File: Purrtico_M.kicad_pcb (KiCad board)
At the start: 2 copper layers, 53 parts, among them J2 Conn_01x02, J3 Conn_01x03, J4 Conn_01x02, U1 OPA1679, U2 OPA1679

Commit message: update pcb
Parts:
- moved R5 89.9 mm to (150.5, 33.7)
- moved R19 82.6 mm to (160.0, 35.6), turned to 180 degrees
- moved R20 72.9 mm to (155.6, 47.6), turned to 180 degrees
- moved R14 67.4 mm to (154.9, 56.5), turned to 180 degrees
- moved R10 65.6 mm to (108.6, 53.3), turned to 0 degrees
- moved R8 63.3 mm to (141.0, 50.8)
- moved C7 60.7 mm to (136.5, 56.5), turned to 90 degrees
- moved C11 60.0 mm to (151.1, 50.8), turned to -90 degrees
- moved R7 59.9 mm to (141.0, 53.3)
- moved R6 55.1 mm to (141.0, 55.9), turned to 180 degrees
- moved R18 52.6 mm to (155.6, 53.3), turned to 0 degrees
- moved R16 52.3 mm to (158.8, 59.1), turned to 0 degrees
- moved R17 50.4 mm to (155.8, 62.2)
- moved R13 43.0 mm to (117.3, 57.1)
- moved C8 10.2 mm to (102.2, 53.3)
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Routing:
- net -15V: track 0.00 -> 73.9 mm
- net +15V: track 0.00 -> 72.9 mm
- net Net-(C7-Pad2): track 0.00 -> 55.7 mm, vias 0 -> 2
- net Net-(C2-Pad1): track 0.00 -> 31.0 mm
- net Net-(C11-Pad1): track 0.00 -> 29.2 mm
- net GND: track 0.00 -> 28.3 mm, vias 0 -> 14
- net Net-(C8-Pad2): track 0.00 -> 26.9 mm
- net Net-(C9-Pad2): track 0.00 -> 25.5 mm
- net Net-(U2B--): track 0.00 -> 24.9 mm
- net Net-(U2C--): track 0.00 -> 18.5 mm
- net Net-(R10-Pad1): track 0.00 -> 18.3 mm
- net Net-(U2A--): track 0.00 -> 16.1 mm
- net Net-(U1D--): track 0.00 -> 14.7 mm
- net Net-(U1B--): track 0.00 -> 13.9 mm
- net Net-(U1A--): track 0.00 -> 13.8 mm
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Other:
- board outline added: 100 x 50 mm

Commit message: update pcb
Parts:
- moved R19 29.2 mm to (130.8, 34.3), turned to 0 degrees
- moved C4 19.7 mm to (135.9, 33.7)
- moved C3 18.7 mm to (122.6, 42.5)
- moved C2 18.0 mm to (134.6, 49.6)
- moved R4 15.3 mm to (135.3, 38.1), turned to 0 degrees
- moved R1 14.7 mm to (123.2, 38.7), turned to 0 degrees
- moved R8 13.4 mm to (139.7, 64.1)
- moved R24 12.9 mm to (151.8, 39.4), turned to 0 degrees
- moved R23 12.7 mm to (109.2, 41.3), turned to 180 degrees
- moved R22 11.0 mm to (151.8, 36.2), turned to 180 degrees
- moved R3 10.8 mm to (119.4, 35.6)
- moved R5 9.67 mm to (141.6, 37.5), turned to 0 degrees
- moved R14 9.61 mm to (153.7, 47.0), turned to 0 degrees
- moved R2 9.61 mm to (152.4, 31.1)
- moved J4 9.55 mm to (144.8, 29.2)
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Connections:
- C3 pad 1: Net-(U1D--) -> Net-(U1C--)
- C4 pad 1: Net-(U2C--) -> Net-(U2D--)
- R1 pad 1: Net-(U1D--) -> Net-(U1C--)
- R14 pad 2: Net-(U2C-+) -> Net-(U2D-+)
- R19 pad 2: Net-(U2C--) -> Net-(U2D--)
- R2 pad 1: Net-(U2C--) -> Net-(U2D--)
- R21 pad 2: Net-(U1C-+) -> Net-(U1D-+)
- R22 pad 2: Net-(U2D-+) -> Net-(U2C-+)
- R23 pad 1: Net-(U1C--) -> Net-(U1D--)
- R24 pad 1: Net-(U2D--) -> Net-(U2C--)
- R3 pad 2: Net-(U1D--) -> Net-(U1C--)
- R4 pad 2: Net-(U2C--) -> Net-(U2D--)
- R5 pad 2: Net-(U2C-+) -> Net-(U2D-+)
- U1 pad 10: Net-(U1C-+) -> GND
- U1 pad 12: GND -> Net-(U1D-+)
- U1 pad 14: Net-(C1-Pad1) -> Net-(R23-Pad2)
- U1 pad 8: Net-(R23-Pad2) -> Net-(C1-Pad1)
- U2 pad 14: Net-(R24-Pad2) -> Net-(C2-Pad1)
- U2 pad 8: Net-(C2-Pad1) -> Net-(R24-Pad2)
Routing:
- net Net-(C8-Pad2): track 26.9 -> 88.1 mm, vias 0 -> 4
- net Net-(C1-Pad1): track 7.44 -> 44.0 mm, vias 0 -> 2
- net Net-(U2D-+): track 6.12 -> 35.0 mm, vias 0 -> 2
- net Net-(U2A--): track 16.1 -> 40.2 mm
- net Net-(C2-Pad1): track 31.0 -> 15.7 mm, vias 0 -> 2
- net Net-(U2C--): track 18.5 -> 3.39 mm
- net Net-(C2-Pad2): track 8.92 -> 22.2 mm
- net Net-(U1D--): track 14.7 -> 2.79 mm
- net Net-(U1C--): track 5.29 -> 15.6 mm
- net Net-(U1C-+): track 6.83 -> 0.00 mm
- net Net-(U1D-+): track 0.00 -> 6.23 mm
- net Net-(U2D--): track 4.37 -> 10.3 mm
- net Net-(J4-Pin_2): track 7.25 -> 13.2 mm
- net Net-(U1A--): track 13.8 -> 9.15 mm
- net Net-(C7-Pad2): track 55.7 -> 59.9 mm
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
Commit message: all connected
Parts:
- moved R2 14.1 mm to (141.0, 39.4), turned to 180 degrees
- moved R5 5.46 mm to (144.8, 33.0), turned to 180 degrees
- moved R19 5.08 mm to (135.9, 34.3)
- moved C4 4.49 mm to (140.3, 33.0)
- moved C6 2.01 mm to (136.5, 29.2)
- moved R4 1.80 mm to (136.5, 36.8)
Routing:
- net Net-(C2-Pad1): track 15.7 -> 35.5 mm
- net Net-(U2D--): track 10.3 -> 14.6 mm
- net Net-(U2D-+): track 35.0 -> 37.3 mm
- net Net-(C1-Pad1): track 44.0 -> 45.8 mm
- net Net-(C8-Pad2): track 88.1 -> 89.3 mm
- net Net-(J4-Pin_2): track 13.2 -> 14.3 mm

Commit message: update pcb
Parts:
- moved R9 30.6 mm to (134.6, 63.5), turned to 0 degrees
- moved C8 19.7 mm to (125.1, 54.6)
- moved C9 17.0 mm to (107.2, 47.2), turned to -90 degrees
- moved R11 16.3 mm to (119.4, 56.5), turned to 180 degrees
- moved R13 10.6 mm to (106.7, 56.4), turned to 0 degrees
- moved R10 8.98 mm to (118.7, 52.1)
- moved R18 8.92 mm to (142.2, 53.8)
- moved R7 5.22 mm to (144.3, 57.4)
- moved C1 4.32 mm to (128.3, 57.9)
- moved R19 3.24 mm to (136.5, 37.5)
- moved C7 2.67 mm to (140.2, 58.9)
- moved C17 2.55 mm to (146.1, 40.0)
- moved C11 2.05 mm to (151.9, 52.7)
- moved R14 2.01 mm to (153.0, 48.9)
- moved C4 2.01 mm to (141.0, 34.9)
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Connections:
- C8 pad 1: Net-(U1A--) -> Net-(U1B--)
- C9 pad 1: Net-(U1B--) -> Net-(U1A--)
- R10 pad 2: Net-(U1A--) -> Net-(U1B--)
- R13 pad 1: Net-(U1B--) -> Net-(U1A--)
- U1 pad 1: Net-(C8-Pad2) -> Net-(C9-Pad2)
- U1 pad 7: Net-(C9-Pad2) -> Net-(C8-Pad2)
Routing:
- net Net-(C7-Pad2): track 59.9 -> 20.6 mm, vias 2 -> 0
- net Net-(C8-Pad2): track 89.3 -> 57.0 mm, vias 4 -> 2
- net Net-(R9-Pad1): track 4.44 -> 26.7 mm
- net Net-(C9-Pad2): track 21.4 -> 35.0 mm, vias 0 -> 2
- net Net-(U2B--): track 23.8 -> 30.7 mm
- net Net-(U2A--): track 40.2 -> 33.7 mm
- net Net-(U1A--): track 9.15 -> 15.5 mm
- net Net-(R8-Pad1): track 4.15 -> 9.91 mm
- net Net-(R13-Pad2): track 10.7 -> 15.8 mm
- net Net-(C1-Pad2): track 7.68 -> 12.8 mm
- net Net-(R11-Pad2): track 8.64 -> 13.6 mm
- net Net-(C11-Pad1): track 28.8 -> 24.6 mm
- net Net-(C1-Pad1): track 45.8 -> 42.5 mm
- net Net-(C2-Pad2): track 22.2 -> 19.8 mm
- net Net-(C2-Pad1): track 35.5 -> 37.7 mm
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
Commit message: update routing
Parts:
- removed J3: Conn_01x03, Connector_PinHeader_2.54mm:PinHeader_1x03_P2.54mm_Vertical
- added J1: Conn_02x05_Odd_Even, Connector_PinHeader_2.54mm:PinHeader_2x05_P2.54mm_Vertical, F.Cu at (181.6, 50.8)
- moved R24 39.9 mm to (113.0, 50.2), turned to 180 degrees
- moved R22 39.8 mm to (115.6, 53.3), turned to 0 degrees
- moved U1 39.4 mm to (153.0, 46.4), turned to -90 degrees
- moved C5 29.3 mm to (142.9, 31.8), turned to -90 degrees
- moved R3 28.7 mm to (148.0, 38.1)
- moved C3 27.9 mm to (149.2, 34.3), turned to 90 degrees
- moved C6 27.4 mm to (165.7, 31.8), turned to -90 degrees
- moved U2 25.4 mm to (120.7, 46.4), turned to -90 degrees
- moved R1 24.8 mm to (148.0, 40.6), turned to 180 degrees
- moved R19 24.7 mm to (160.7, 42.5), turned to 180 degrees
- moved C2 23.6 mm to (154.3, 61.6)
- moved C9 22.4 mm to (127.6, 38.1)
- moved R13 21.6 mm to (128.3, 57.1), turned to 180 degrees
- moved R4 21.0 mm to (157.5, 34.9)
- moved R2 19.7 mm to (160.0, 32.4), turned to 0 degrees
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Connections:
- C11 pad 2: Net-(U2B--) -> Net-(U1D--)
- C13 pad 1: +15V -> -15V
- C14 pad 1: +15V -> -15V
- C16 pad 2: -15V -> +15V
- C17 pad 2: -15V -> +15V
- C3 pad 1: Net-(U1C--) -> Net-(U1B--)
- C4 pad 1: Net-(U2D--) -> Net-(U1A--)
- C7 pad 1: Net-(U2A--) -> Net-(U1C--)
- C8 pad 1: Net-(U1B--) -> Net-(U2D--)
- C9 pad 1: Net-(U1A--) -> Net-(U2A--)
- R1 pad 1: Net-(U1C--) -> Net-(U1B--)
- R10 pad 2: Net-(U1B--) -> Net-(U2D--)
- R13 pad 1: Net-(U1A--) -> Net-(U2A--)
- R14 pad 2: Net-(U2D-+) -> Net-(U1A-+)
- R17 pad 2: Net-(U2B--) -> Net-(U1D--)
- R18 pad 1: Net-(U2B--) -> Net-(U1D--)
- R19 pad 2: Net-(U2D--) -> Net-(U1A--)
- R2 pad 1: Net-(U2D--) -> Net-(U1A--)
- R20 pad 1: Net-(U2A--) -> Net-(U1C--)
- R21 pad 2: Net-(U1D-+) -> Net-(U2B-+)
- R23 pad 1: Net-(U1D--) -> Net-(U2B--)
- R3 pad 2: Net-(U1C--) -> Net-(U1B--)
- R4 pad 2: Net-(U2D--) -> Net-(U1A--)
- R5 pad 2: Net-(U2D-+) -> Net-(U1A-+)
- R6 pad 1: Net-(U2A--) -> Net-(U1C--)
- R7 pad 1: Net-(U2A--) -> Net-(U1C--)
- R8 pad 2: Net-(U2A--) -> Net-(U1C--)
- RV3 pad 1: Net-(U2B--) -> Net-(U1D--)
- U1 pad 1: Net-(C9-Pad2) -> Net-(C2-Pad1)
- U1 pad 12: Net-(U1D-+) -> GND
- U1 pad 14: Net-(R23-Pad2) -> Net-(C11-Pad1)
- U1 pad 3: GND -> Net-(U1A-+)
- U1 pad 7: Net-(C8-Pad2) -> Net-(C1-Pad1)
- U1 pad 8: Net-(C1-Pad1) -> Net-(C7-Pad2)
- U2 pad 1: Net-(C7-Pad2) -> Net-(C9-Pad2)
- U2 pad 12: Net-(U2D-+) -> GND
- U2 pad 14: Net-(C2-Pad1) -> Net-(C8-Pad2)
- U2 pad 5: GND -> Net-(U2B-+)
- U2 pad 7: Net-(C11-Pad1) -> Net-(R23-Pad2)
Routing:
- net Net-(U2D-+): track 38.4 -> 0.00 mm, vias 2 -> 0
- net Net-(U2B--): track 30.7 -> 2.88 mm
- net Net-(C2-Pad1): track 37.7 -> 64.4 mm, vias 2 -> 4
- net Net-(U1D--): track 2.79 -> 26.0 mm
- net Net-(U1A-+): track 0.00 -> 20.7 mm, vias 0 -> 2
- net Net-(U1C--): track 15.6 -> 32.1 mm
- net Net-(C2-Pad2): track 19.8 -> 8.12 mm
- net Net-(C7-Pad2): track 20.6 -> 9.23 mm
- net Net-(R9-Pad1): track 26.7 -> 36.9 mm
- net Net-(C9-Pad2): track 35.0 -> 25.6 mm
- net GND: track 28.1 -> 37.0 mm, vias 14 -> 18
- net Net-(J4-Pin_2): track 12.4 -> 19.8 mm
- net Net-(C8-Pad2): track 57.0 -> 64.2 mm, vias 2 -> 4
- net Net-(R11-Pad2): track 13.6 -> 20.6 mm
- net Net-(U2B-+): track 0.00 -> 6.92 mm
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
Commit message: Update Purrtico_M.kicad_pcb
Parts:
- moved R13 4.44 mm to (132.7, 57.1)
- moved R10 3.81 mm to (132.7, 54.0)
- moved R15 3.42 mm to (135.3, 61.6)
- moved R12 2.62 mm to (135.3, 64.1)
- moved C8 2.29 mm to (126.4, 59.1)
- moved C9 2.02 mm to (129.5, 37.5)
- moved R5 0.63 mm to (160.7, 38.7)
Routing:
- net Net-(U2D--): track 15.2 -> 21.4 mm
- net Net-(R11-Pad2): track 20.6 -> 24.8 mm
- net Net-(C8-Pad2): track 64.2 -> 66.3 mm
- net Net-(U2A--): track 38.4 -> 36.5 mm
- net Net-(R13-Pad2): track 16.7 -> 18.6 mm
- net Net-(R10-Pad1): track 17.3 -> 18.8 mm
- net Net-(R15-Pad2): track 7.41 -> 8.58 mm
- net GND: track 37.0 -> 35.8 mm
- net Net-(C2-Pad1): track 64.4 -> 63.3 mm
- net Net-(C11-Pad1): track 30.3 -> 29.2 mm
- net Net-(R9-Pad1): track 36.9 -> 35.9 mm
- net Net-(U1A-+): track 20.7 -> 21.6 mm
- net Net-(U1D--): track 26.0 -> 25.3 mm
- net Net-(U1A--): track 17.2 -> 16.6 mm
- net Net-(R23-Pad2): track 3.56 -> 2.97 mm
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
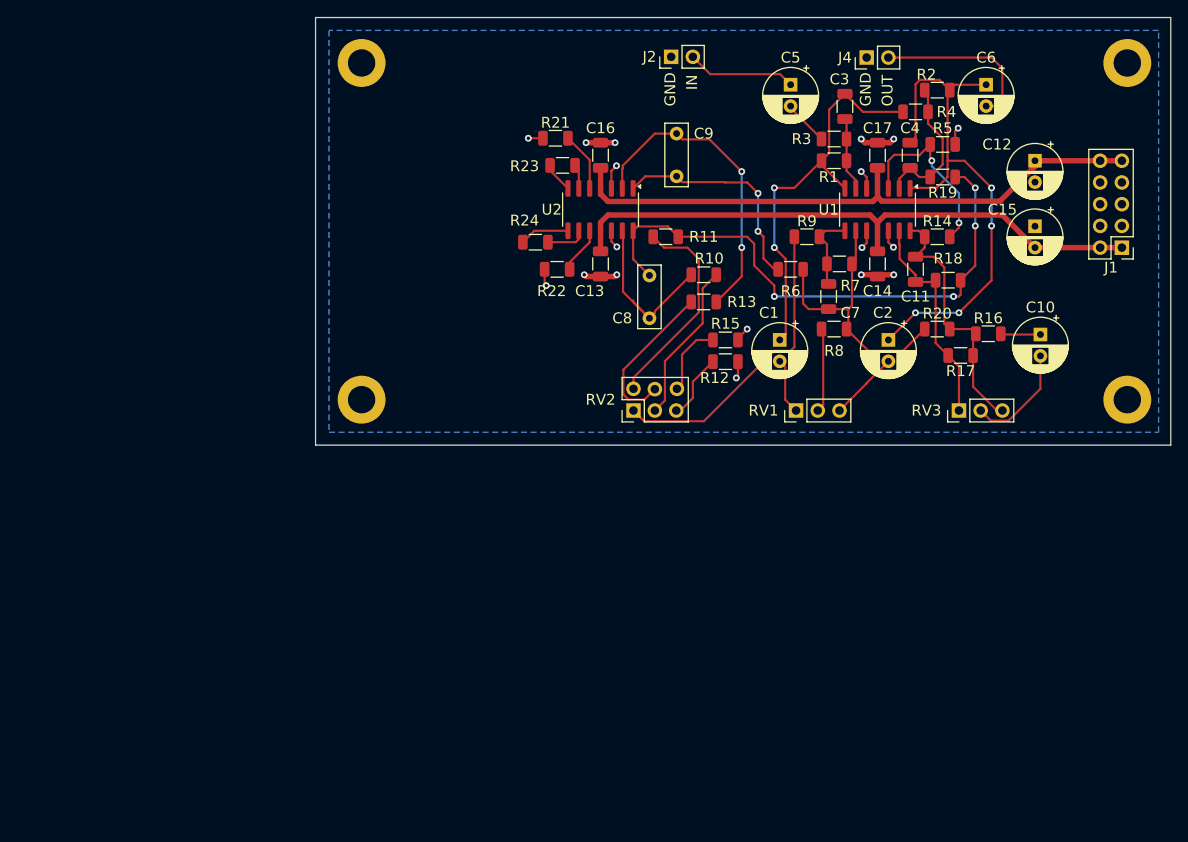
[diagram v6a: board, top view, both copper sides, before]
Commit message: added shelving band
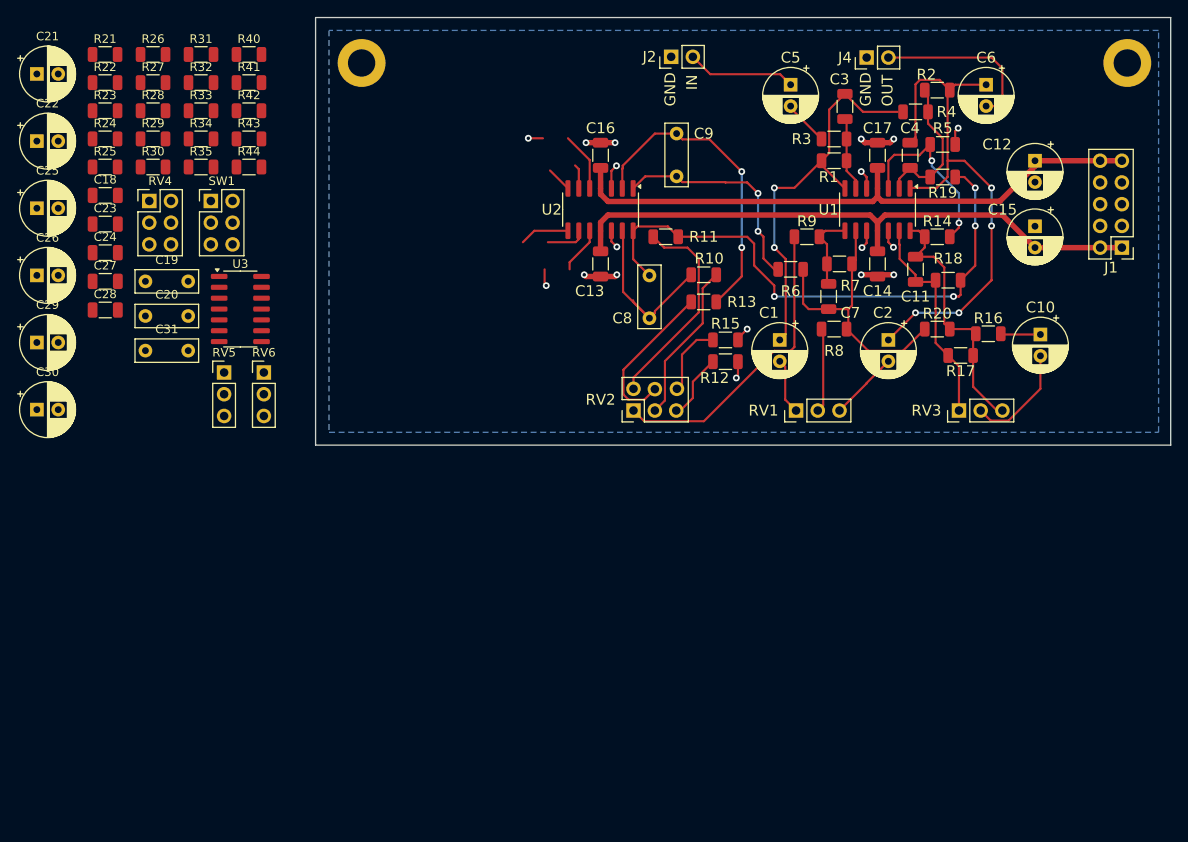
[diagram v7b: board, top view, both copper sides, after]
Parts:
- removed H3, H4: MountingHole, MountingHole:MountingHole_3.2mm_M3_DIN965_Pad
- added C18: 22p, Capacitor_SMD:C_1206_3216Metric, F.Cu at (62.7, 44.7)
- added C19: 5n6, Capacitor_THT:C_Rect_L7.2mm_W2.5mm_P5.00mm_FKS2_FKP2_MKS2_MKP2, F.Cu at (67.4, 54.7)
- added C20: 470n, Capacitor_THT:C_Rect_L7.2mm_W2.5mm_P5.00mm_FKS2_FKP2_MKS2_MKP2, F.Cu at (67.4, 58.8)
- added C21: 22u, Capacitor_THT:CP_Radial_D6.3mm_P2.50mm, F.Cu at (54.7, 30.5)
- added C22: 100u, Capacitor_THT:CP_Radial_D6.3mm_P2.50mm, F.Cu at (54.7, 38.3)
- added C23: 100n, Capacitor_SMD:C_1206_3216Metric, F.Cu at (62.7, 48.0)
- added C24: 100n, Capacitor_SMD:C_1206_3216Metric, F.Cu at (62.7, 51.4)
- added C25: 100u, Capacitor_THT:CP_Radial_D6.3mm_P2.50mm, F.Cu at (54.7, 46.2)
- added C26: 100u, Capacitor_THT:CP_Radial_D6.3mm_P2.50mm, F.Cu at (54.7, 54.0)
- added C27: 100p, Capacitor_SMD:C_1206_3216Metric, F.Cu at (62.7, 54.7)
- added C28: 100p, Capacitor_SMD:C_1206_3216Metric, F.Cu at (62.7, 58.1)
- added C29: 100u, Capacitor_THT:CP_Radial_D6.3mm_P2.50mm, F.Cu at (54.7, 61.9)
- added C30: 100u, Capacitor_THT:CP_Radial_D6.3mm_P2.50mm, F.Cu at (54.7, 69.7)
- added C31: 470n, Capacitor_THT:C_Rect_L7.2mm_W2.5mm_P5.00mm_FKS2_FKP2_MKS2_MKP2, F.Cu at (67.4, 62.8)
- added R25: 2k2, Resistor_SMD:R_1206_3216Metric, F.Cu at (62.7, 41.4)
- added R26: 12k, Resistor_SMD:R_1206_3216Metric, F.Cu at (68.3, 28.2)
- added R27: 0R, Resistor_SMD:R_1206_3216Metric, F.Cu at (68.3, 31.5)
- added R28: 100R, Resistor_SMD:R_1206_3216Metric, F.Cu at (68.3, 34.8)
- added R29: 1k5, Resistor_SMD:R_1206_3216Metric, F.Cu at (68.3, 38.1)
- added R30: 100R, Resistor_SMD:R_1206_3216Metric, F.Cu at (68.3, 41.4)
- added R31: 390R, Resistor_SMD:R_1206_3216Metric, F.Cu at (73.9, 28.2)
- added R32: 1k5, Resistor_SMD:R_1206_3216Metric, F.Cu at (73.9, 31.5)
- added R33: 0R, Resistor_SMD:R_1206_3216Metric, F.Cu at (73.9, 34.8)
- added R34: 390R, Resistor_SMD:R_1206_3216Metric, F.Cu at (73.9, 38.1)
- added R35: 1M, Resistor_SMD:R_1206_3216Metric, F.Cu at (73.9, 41.4)
- added R40: 2k7, Resistor_SMD:R_1206_3216Metric, F.Cu at (79.5, 28.2)
- added R41: 2k7, Resistor_SMD:R_1206_3216Metric, F.Cu at (79.5, 31.5)
- added R42: 2k7, Resistor_SMD:R_1206_3216Metric, F.Cu at (79.5, 34.8)
- added R43: 2k7, Resistor_SMD:R_1206_3216Metric, F.Cu at (79.5, 38.1)
- added R44: 18k, Resistor_SMD:R_1206_3216Metric, F.Cu at (79.5, 41.4)
- added RV4: 10k, Connector_PinHeader_2.54mm:PinHeader_2x03_P2.54mm_Vertical, F.Cu at (67.9, 45.3)
- added RV5: 10k, Connector_PinHeader_2.54mm:PinHeader_1x03_P2.54mm_Vertical, F.Cu at (76.6, 65.4)
- added RV6: 4k7, Connector_PinHeader_2.54mm:PinHeader_1x03_P2.54mm_Vertical, F.Cu at (81.3, 65.4)
- added SW1: SW_DPDT_x2, Connector_PinHeader_2.54mm:PinHeader_2x03_P2.54mm_Vertical, F.Cu at (75.1, 45.3)
- added U3: OPA1679, Package_SO:SOIC-14_3.9x8.7mm_P1.27mm, F.Cu at (78.5, 58.0)
- R21, R22: value 0R -> 3M3
- R23: value 0R -> 2k2
- R24: value 0R -> 560R
- moved R22 57.2 mm to (62.7, 31.5)
- moved R23 53.9 mm to (62.7, 34.8), turned to 0 degrees
- moved R21 53.6 mm to (62.7, 28.2)
- moved R24 51.7 mm to (62.7, 38.1), turned to 0 degrees
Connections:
- C5 pad 1: Net-(J2-Pin_2) -> Net-(C30-Pad2)
- R21 pad 2: Net-(U2B-+) -> Net-(SW1B-B)
- R22 pad 1: GND -> Net-(SW1B-B)
- R22 pad 2: Net-(U2C-+) -> Net-(R22-Pad2)
- R23 pad 1: Net-(U2B--) -> Net-(SW1B-A)
- R23 pad 2: Net-(R23-Pad2) -> Net-(R22-Pad2)
- R24 pad 1: Net-(U2C--) -> Net-(R24-Pad1)
- R24 pad 2: Net-(R24-Pad2) -> Net-(SW1B-C)
- U2 pad 5: Net-(U2B-+) -> GND
- U2 pad 7: Net-(R23-Pad2) -> Net-(C25-Pad1)
- U2 pad 8: Net-(R24-Pad2) -> Net-(C28-Pad2)
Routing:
- net Net-(U2B-+): track 6.92 -> 0.00 mm
- net GND: track 35.8 -> 42.8 mm
- net Net-(R24-Pad2): track 5.83 -> 0.00 mm
- net Net-(C28-Pad2): track 0.00 -> 5.83 mm
- net Net-(R23-Pad2): track 2.97 -> 0.00 mm
- net Net-(C25-Pad1): track 0.00 -> 2.97 mm

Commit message: modified shelving filter
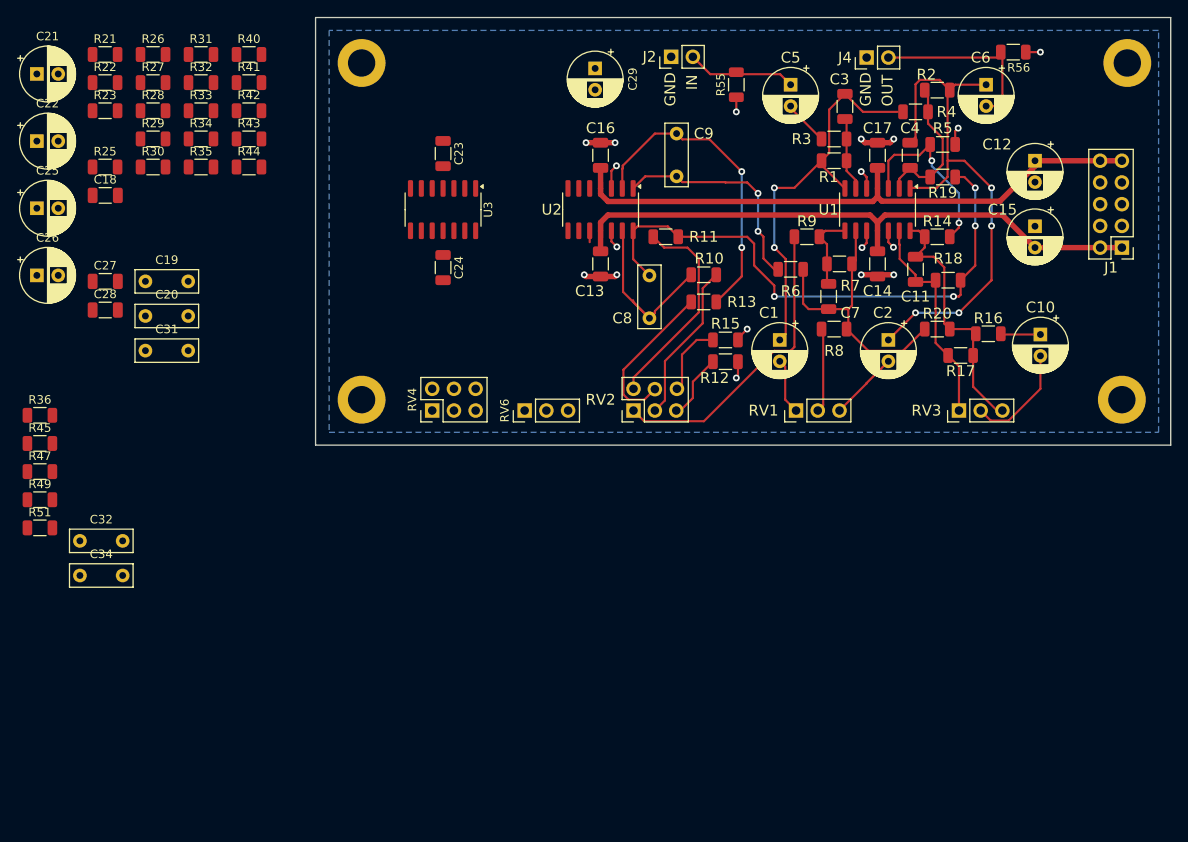
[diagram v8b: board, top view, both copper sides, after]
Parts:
- removed C30: 100u, Capacitor_THT:CP_Radial_D6.3mm_P2.50mm
- removed R24: 560R, Resistor_SMD:R_1206_3216Metric
- removed RV5: 10k, Connector_PinHeader_2.54mm:PinHeader_1x03_P2.54mm_Vertical
- removed SW1: SW_DPDT_x2, Connector_PinHeader_2.54mm:PinHeader_2x03_P2.54mm_Vertical
- added C32: 680n, Capacitor_THT:C_Rect_L7.2mm_W2.5mm_P5.00mm_FKS2_FKP2_MKS2_MKP2, F.Cu at (59.8, 85.1)
- added C34: 68n, Capacitor_THT:C_Rect_L7.2mm_W2.5mm_P5.00mm_FKS2_FKP2_MKS2_MKP2, F.Cu at (59.8, 89.1)
- added H3: MountingHole, MountingHole:MountingHole_3.2mm_M3_DIN965_Pad, F.Cu at (92.7, 68.6)
- added H4: MountingHole, MountingHole:MountingHole_3.2mm_M3_DIN965_Pad, F.Cu at (181.6, 68.6)
- added R36: 4k7, Resistor_SMD:R_1206_3216Metric, F.Cu at (55.1, 70.4)
- added R45: 0R, Resistor_SMD:R_1206_3216Metric, F.Cu at (55.1, 73.7)
- added R47: 0R, Resistor_SMD:R_1206_3216Metric, F.Cu at (55.1, 77.0)
- added R49: 0R, Resistor_SMD:R_1206_3216Metric, F.Cu at (55.1, 80.3)
- added R51: 0R, Resistor_SMD:R_1206_3216Metric, F.Cu at (55.1, 83.6)
- added R55: 100k, Resistor_SMD:R_1206_3216Metric, F.Cu at (136.5, 31.8)
- added R56: 100k, Resistor_SMD:R_1206_3216Metric, F.Cu at (168.9, 27.9)
- C19: value 5n6 -> 68n
- moved C29 72.7 mm to (120.0, 29.8), turned to -90 degrees
- moved RV4 41.2 mm to (101.0, 69.8), turned to 90 degrees
- moved C23 40.4 mm to (102.2, 39.8), turned to -90 degrees
- moved C24 39.5 mm to (102.2, 53.1), turned to -90 degrees
- moved RV6 30.8 mm to (111.8, 69.8), turned to 90 degrees
- moved U3 26.4 mm to (102.2, 46.4), turned to -90 degrees
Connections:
- C22 pad 1: Net-(SW1B-B) -> Net-(C22-Pad1)
- C26 pad 2: Net-(U3A-+) -> Net-(C26-Pad2)
- C5 pad 1: Net-(C30-Pad2) -> Net-(C28-Pad2)
- R21 pad 2: Net-(SW1B-B) -> Net-(C22-Pad1)
- R22 pad 1: Net-(SW1B-B) -> Net-(C22-Pad1)
- R23 pad 1: Net-(SW1B-A) -> Net-(C22-Pad1)
- R28 pad 2: Net-(C18-Pad2) -> Net-(R28-Pad2)
- U3 pad 1: Net-(C18-Pad2) -> Net-(R28-Pad2)
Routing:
- net GND: track 42.8 -> 35.6 mm
- net Net-(C28-Pad2): track 5.83 -> 0.00 mm
- net Net-(U2C--): track 4.74 -> 0.00 mm
- net Net-(U2C-+): track 5.48 -> 1.34 mm
- net Net-(C25-Pad1): track 2.97 -> 0.00 mm
- net Net-(U2B--): track 2.88 -> 0.00 mm
- net Net-(J4-Pin_2): track 19.8 -> 20.6 mm
